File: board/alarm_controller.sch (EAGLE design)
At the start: 142 parts, among them IC3 AT24C, X1 RJ45-8L21-S, X2 RJ45-8L21-S

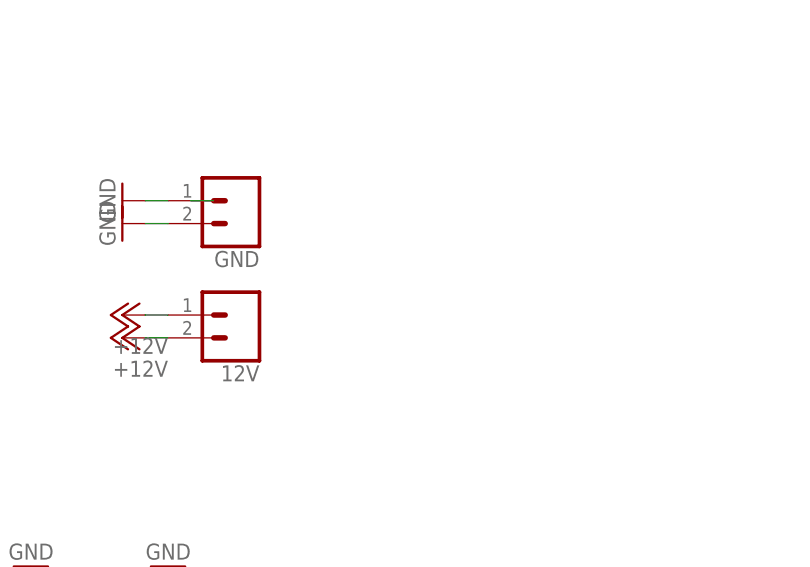
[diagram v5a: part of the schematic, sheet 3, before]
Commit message: increase 12v and gnd connections
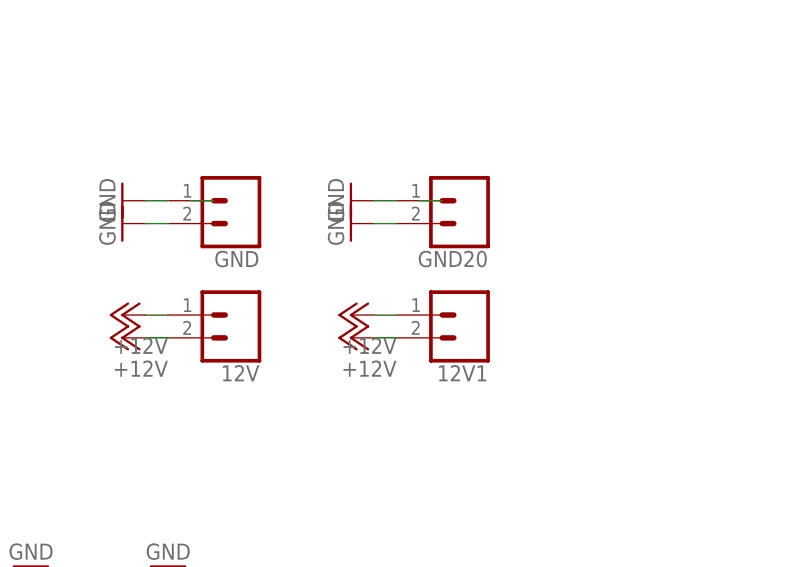
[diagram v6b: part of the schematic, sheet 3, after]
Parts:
- added 12V1, GND20: (no value), SparkFun-Connectors:CONN_023.5MM
- GND8: device SparkFun-Connectors:CONN_023.5MM -> SparkFun-Connectors:CONN_025MM
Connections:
- net +12V: now also 12V1.1, 12V1.2
- net GND: now also GND20.1, GND20.2

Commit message: jumpers for boot mode
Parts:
- removed PAD1, PAD2: WIREPADSMD5-1,8, wirepad:WIREPADSMD5-1,8
- removed R2: 10k, rcl:R-EU_R0603
- added JP2: (no value), jumper:JP3Q
- added R63, R64, R65, R66: 10k, rcl:R-EU_R0603
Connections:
- removed net N$12: PAD2.P, R2.2, U$1.BOOT0
- new net BOOT0: JP2.3, U$1.BOOT0
- new net BOOT1: JP2.4, U$1.PB2
- new net N$13: JP2.1, R64.1
- new net N$14: JP2.6, R65.1
- new net N$15: JP2.5, R63.1
- new net N$5: JP2.2, R66.1
- net +3V3: now also R64.2, R66.2; no longer PAD1.P
- net GND: now also R63.2, R65.2; no longer R2.1

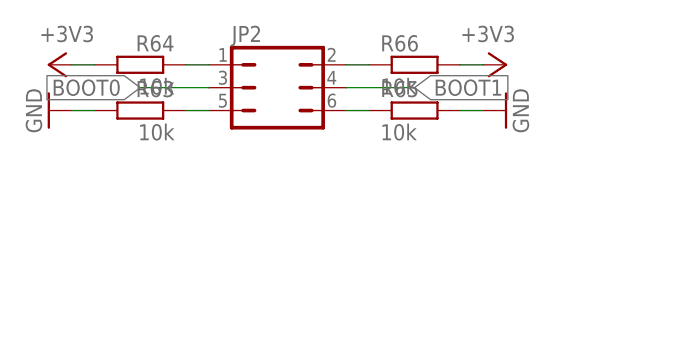
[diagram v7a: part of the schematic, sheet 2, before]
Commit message: change to solderable boot jumper
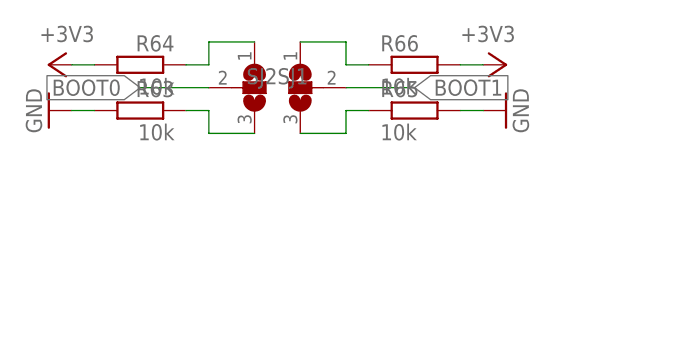
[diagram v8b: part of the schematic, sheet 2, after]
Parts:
- removed JP2: (no value), jumper:JP3Q
- added SJ1, SJ2: (no value), jumper:SJ2W
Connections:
- net BOOT0: now also SJ1.2; no longer JP2.3
- net BOOT1: now also SJ2.2; no longer JP2.4
- net N$13: now also SJ1.1; no longer JP2.1
- net N$14: now also SJ2.3; no longer JP2.6
- net N$15: now also SJ1.3; no longer JP2.5
- net N$5: now also SJ2.1; no longer JP2.2
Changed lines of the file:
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@@
 <part name="+3V33" library="supply1" deviceset="+3V3" device=""/>
 <part name="+3V34" library="supply1" deviceset="+3V3" device=""/>
-<part name="JP2" library="jumper" deviceset="JP3Q" device=""/>
+<part name="SJ1" library="jumper" deviceset="SJ2W" device=""/>
+<part name="SJ2" library="jumper" deviceset="SJ2W" device=""/>
 </parts>
 <sheets>
@@
 <instance part="+3V33" gate="G$1" x="-167.64" y="144.78" rot="MR270"/>
 <instance part="+3V34" gate="G$1" x="-116.84" y="144.78" rot="R270"/>
-<instance part="JP2" gate="B" x="-142.24" y="142.24" rot="R270"/>
+<instance part="SJ1" gate="G$1" x="-144.78" y="142.24"/>
+<instance part="SJ2" gate="G$1" x="-139.7" y="142.24" rot="MR0"/>
 </instances>
 <busses>
@@
 <wire x1="-134.62" y1="142.24" x2="-127" y2="142.24" width="0.1524" layer="91"/>
 <label x="-127" y="142.24" size="1.778" layer="95" xref="yes"/>
-<pinref part="JP2" gate="B" pin="4"/>
+<pinref part="SJ2" gate="G$1" pin="2"/>
 </segment>
 <segment>
@@
 <wire x1="-149.86" y1="142.24" x2="-157.48" y2="142.24" width="0.1524" layer="91"/>
 <label x="-157.48" y="142.24" size="1.778" layer="95" rot="MR0" xref="yes"/>
-<pinref part="JP2" gate="B" pin="3"/>
+<pinref part="SJ1" gate="G$1" pin="2"/>
 </segment>
 <segment>
@@
 <wire x1="-134.62" y1="144.78" x2="-132.08" y2="144.78" width="0.1524" layer="91"/>
 <pinref part="R66" gate="G$1" pin="1"/>
-<pinref part="JP2" gate="B" pin="2"/>
+<pinref part="SJ2" gate="G$1" pin="1"/>
+<wire x1="-139.7" y1="147.32" x2="-134.62" y2="147.32" width="0.1524" layer="91"/>
+<wire x1="-134.62" y1="147.32" x2="-134.62" y2="144.78" width="0.1524" layer="91"/>
 </segment>
 </net>
@@
 <wire x1="-149.86" y1="144.78" x2="-152.4" y2="144.78" width="0.1524" layer="91"/>
 <pinref part="R64" gate="G$1" pin="1"/>
-<pinref part="JP2" gate="B" pin="1"/>
+<pinref part="SJ1" gate="G$1" pin="1"/>
+<wire x1="-144.78" y1="147.32" x2="-149.86" y2="147.32" width="0.1524" layer="91"/>
+<wire x1="-149.86" y1="147.32" x2="-149.86" y2="144.78" width="0.1524" layer="91"/>
 </segment>
 </net>
@@
 <wire x1="-134.62" y1="139.7" x2="-132.08" y2="139.7" width="0.1524" layer="91"/>
 <pinref part="R65" gate="G$1" pin="1"/>
-<pinref part="JP2" gate="B" pin="6"/>
+<pinref part="SJ2" gate="G$1" pin="3"/>
+<wire x1="-139.7" y1="137.16" x2="-134.62" y2="137.16" width="0.1524" layer="91"/>
+<wire x1="-134.62" y1="137.16" x2="-134.62" y2="139.7" width="0.1524" layer="91"/>
 </segment>
 </net>
@@
 <wire x1="-149.86" y1="139.7" x2="-152.4" y2="139.7" width="0.1524" layer="91"/>
 <pinref part="R63" gate="G$1" pin="1"/>
-<pinref part="JP2" gate="B" pin="5"/>
-</segment>
-</net>
+<pinref part="SJ1" gate="G$1" pin="3"/>
+<wire x1="-144.78" y1="137.16" x2="-149.86" y2="137.16" width="0.1524" layer="91"/>
+<wire x1="-149.86" y1="137.16" x2="-149.86" y2="139.7" width="0.1524" layer="91"/>
+</segment>
+</net>
